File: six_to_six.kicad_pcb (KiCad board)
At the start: 2 copper layers, 114.3 x 77.5 mm, 73 parts, among them J1 BNC, J2 limiter, J3 Relay control, J4 RF Conn, K1 RY-12W-K, K2 RY-12W-K, K3 RY-12W-K, K4 RY-12W-K, K5 RY-12W-K, K6 RY-12W-K, Q1 MMBT3904, Q2 MMBT3904, Q3 MMBT3904, Q4 MMBT3904, Q5 MMBT3904, Q6 MMBT3904

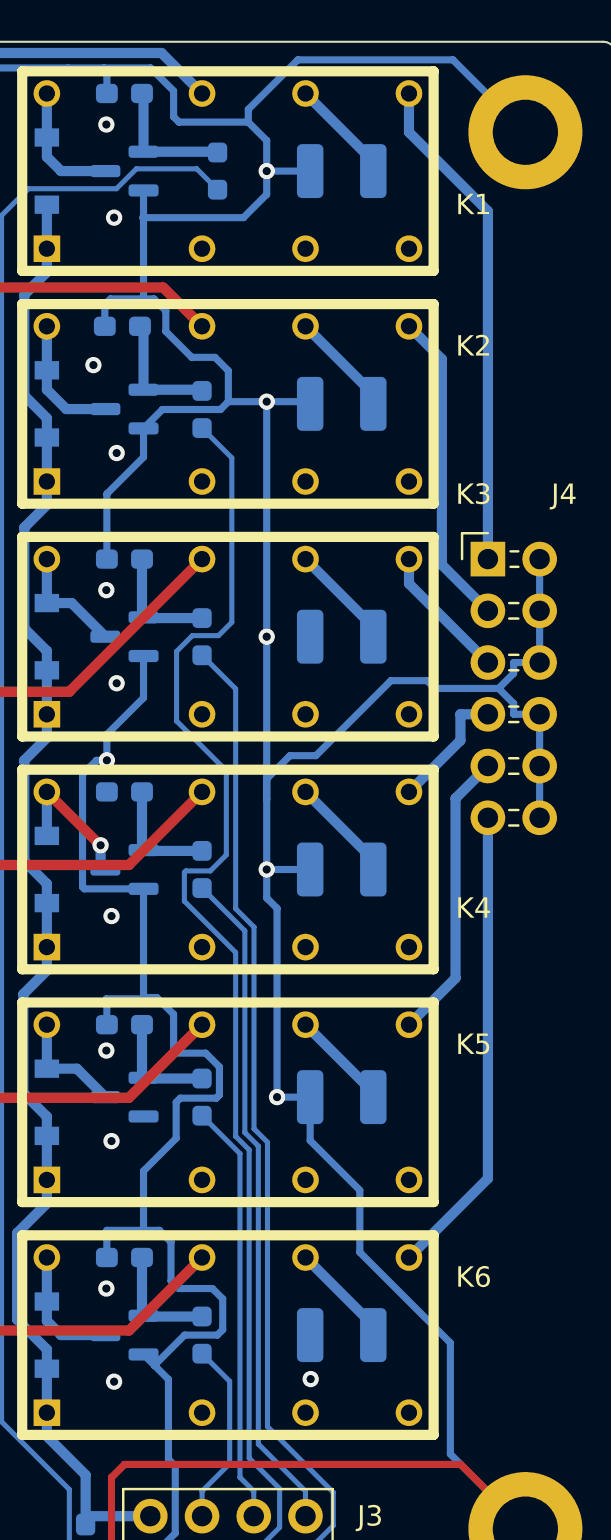
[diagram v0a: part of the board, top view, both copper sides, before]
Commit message: used both contacts on relays
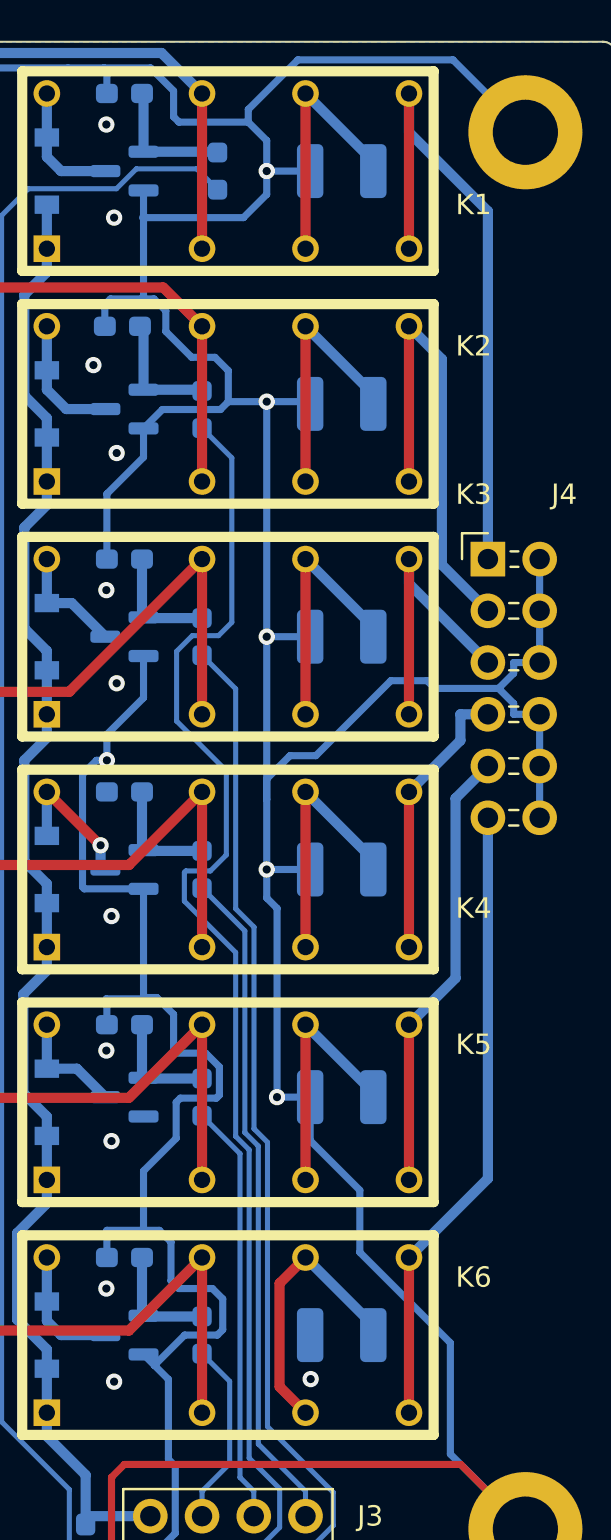
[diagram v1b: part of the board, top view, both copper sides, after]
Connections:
- K1 pad 4: unconnected-(K1-Pad4) -> /2-Way Splitter1/RF-out-1
- K1 pad 6: unconnected-(K1-Pad6) -> Net-(K1-Pad11)
- K1 pad 8: unconnected-(K1-Pad8) -> /Connectors/RF-1
- K2 pad 4: unconnected-(K2-Pad4) -> /2-Way Splitter1/RF-out-2
- K2 pad 6: unconnected-(K2-Pad6) -> Net-(K2-Pad11)
- K2 pad 8: unconnected-(K2-Pad8) -> /Connectors/RF-2
- K3 pad 4: unconnected-(K3-Pad4) -> /2-Way Splitter2/RF-out-1
- K3 pad 6: unconnected-(K3-Pad6) -> Net-(K3-Pad11)
- K3 pad 8: unconnected-(K3-Pad8) -> /Connectors/RF-3
- K4 pad 4: unconnected-(K4-Pad4) -> /2-Way Splitter2/RF-out-2
- K4 pad 6: unconnected-(K4-Pad6) -> Net-(K4-Pad11)
- K4 pad 8: unconnected-(K4-Pad8) -> /Connectors/RF-4
- K5 pad 4: unconnected-(K5-Pad4) -> /2-Way Splitter3/RF-out-1
- K5 pad 6: unconnected-(K5-Pad6) -> Net-(K5-Pad11)
- K5 pad 8: unconnected-(K5-Pad8) -> /Connectors/RF-5
- K6 pad 4: unconnected-(K6-Pad4) -> /2-Way Splitter3/RF-out-2
- K6 pad 6: unconnected-(K6-Pad6) -> Net-(K6-Pad11)
- K6 pad 8: unconnected-(K6-Pad8) -> /Connectors/RF-6
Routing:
- net Net-(K6-Pad11): track 5.19 -> 13.9 mm
- net /2-Way Splitter2/RF-out-2: track 56.6 -> 64.2 mm
- net /2-Way Splitter2/RF-out-1: track 58.2 -> 65.8 mm
- net Net-(K4-Pad11): track 5.19 -> 12.8 mm
- net Net-(K3-Pad11): track 5.19 -> 12.8 mm
- net Net-(K2-Pad11): track 5.19 -> 12.8 mm
- net /Connectors/RF-3: track 6.69 -> 14.3 mm
- net /Connectors/RF-6: track 23.2 -> 30.8 mm
- net /Connectors/RF-4: track 6.21 -> 13.8 mm
- net /Connectors/RF-2: track 15.6 -> 23.2 mm
- net /2-Way Splitter3/RF-out-2: track 53.4 -> 61.1 mm
- net /2-Way Splitter1/RF-out-2: track 48.6 -> 56.2 mm
- net /Connectors/RF-5: track 14.3 -> 21.9 mm
- net Net-(K5-Pad11): track 4.93 -> 12.6 mm
- net /Connectors/RF-1: track 24.5 -> 32.1 mm
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
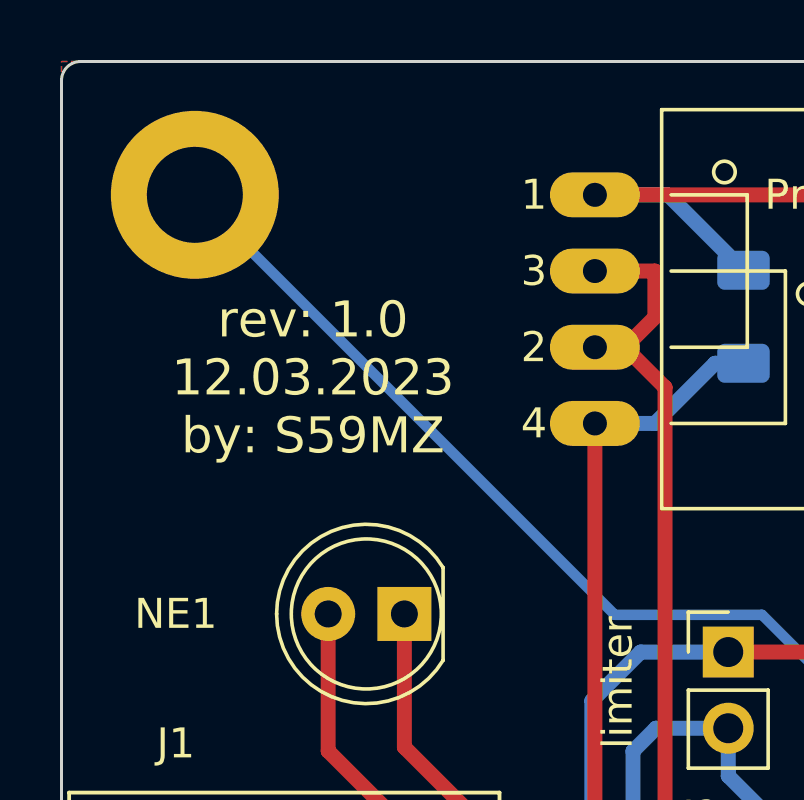
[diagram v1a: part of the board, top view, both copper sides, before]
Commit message: move mounting hole mere inside
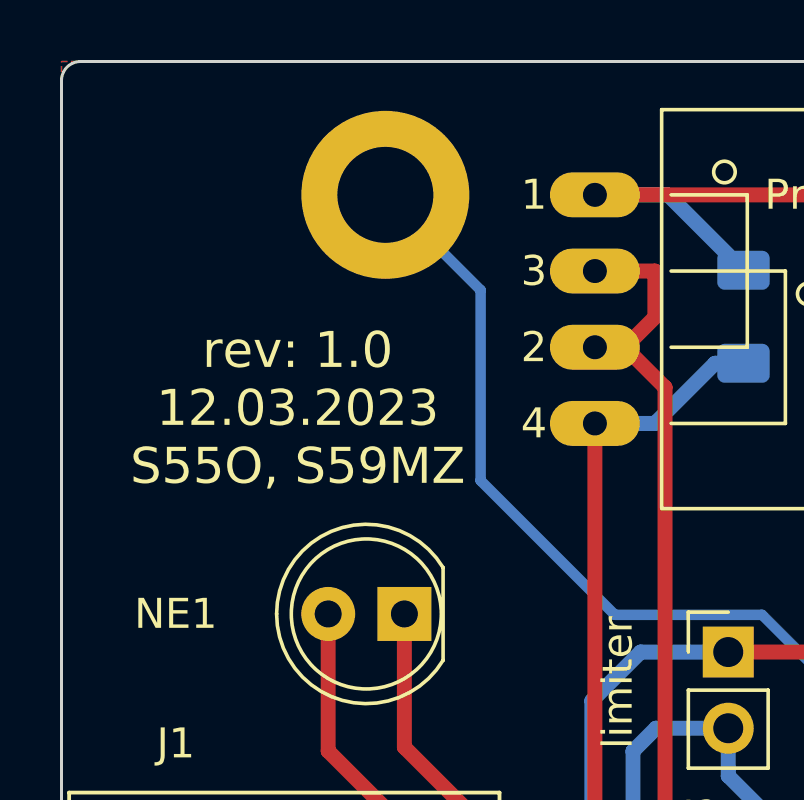
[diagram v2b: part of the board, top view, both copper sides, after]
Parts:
- moved H1 6.35 mm to (652.1, 163.8)
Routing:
- net GND: track 521.4 -> 518.7 mm
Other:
- board text added: "rev: 1.0 12.03.2023 S55O, S59MZ"
- board text removed: "rev: 1.0 12.03.2023 by: S59MZ"
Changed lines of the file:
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@@
   )
   (footprint "MountingHole:MountingHole_3.2mm_M3_DIN965_Pad" locked (layer "F.Cu")
-    (at 645.795 163.83)
+    (at 652.145 163.83)
     (descr "Mounting Hole 3.2mm, M3, DIN965")
     (tags "mounting hole 3.2mm m3 din965")
@@
   (gr_line locked (start 641.35 160.02) (end 641.35 236.22) (layer "Edge.Cuts") (width 0.1))
   (gr_line locked (start 755.65 160.02) (end 755.65 236.22) (layer "Edge.Cuts") (width 0.1))
-  (gr_text "rev: 1.0\n12.03.2023\nby: S59MZ" (at 649.732 169.926) (layer "F.SilkS")
+  (gr_text "rev: 1.0\n12.03.2023\nS55O, S59MZ" (at 649.224 170.942) (layer "F.SilkS")
     (effects (font (size 1.2 1.2) (thickness 0.15)))
   )
@@
   (segment (start 732.9915 224.3695) (end 734.477 222.884) (width 0.35) (layer "B.Cu") (net 1))
   (segment (start 751.905 189.865) (end 750.63 189.865) (width 0.35) (layer "B.Cu") (net 1))
+  (segment (start 655.32 173.355) (end 659.794 177.829) (width 0.35) (layer "B.Cu") (net 1))
   (segment (start 746.76 191.135) (end 746.379 190.754) (width 0.35) (layer "B.Cu") (net 1))
   (segment (start 737.6 163.331) (end 737.6 162.707) (width 0.35) (layer "B.Cu") (net 1))
   (segment (start 659.13 234.95) (end 684.149 234.95) (width 0.35) (layer "B.Cu") (net 1))
+  (segment (start 655.32 167.005) (end 655.32 173.355) (width 0.35) (layer "B.Cu") (net 1))
   (segment (start 738.505 164.236) (end 737.6 163.331) (width 0.35) (layer "B.Cu") (net 1))
   (segment (start 738.505 177.055) (end 738.505 188.595) (width 0.35) (layer "B.Cu") (net 1))
   (segment (start 728.742 160.671) (end 723.904 160.671) (width 0.35) (layer "B.Cu") (net 1))
-  (segment (start 645.795 163.83) (end 659.794 177.829) (width 0.35) (layer "B.Cu") (net 1))
   (segment (start 733.933 207.137) (end 733.107 206.311) (width 0.35) (layer "B.Cu") (net 1))
+  (segment (start 652.145 163.83) (end 655.32 167.005) (width 0.35) (layer "B.Cu") (net 1))
   (segment (start 730.52 160.671) (end 728.742 160.671) (width 0.35) (layer "B.Cu") (net 1))
   (segment (start 687.302 231.797) (end 687.302 226.59) (width 0.35) (layer "B.Cu") (net 1))

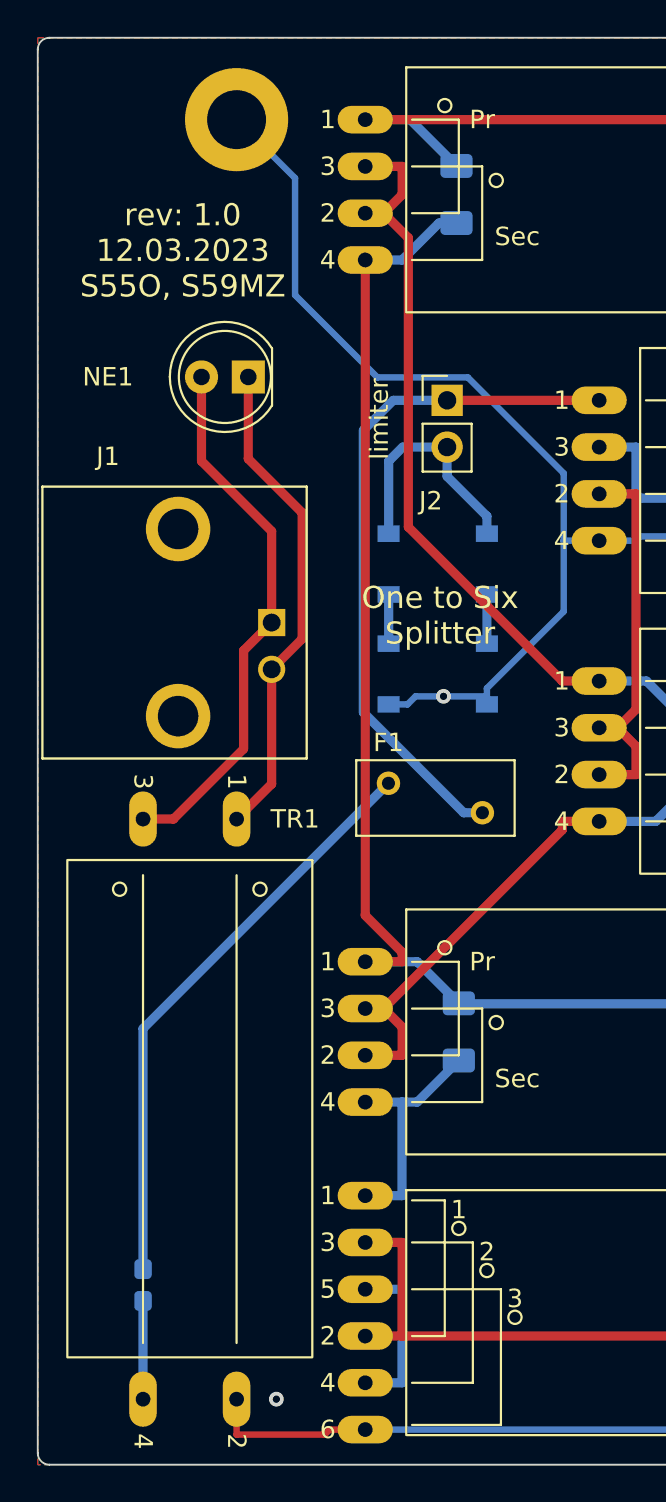
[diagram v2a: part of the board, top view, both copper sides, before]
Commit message: update CMM footprint and board name
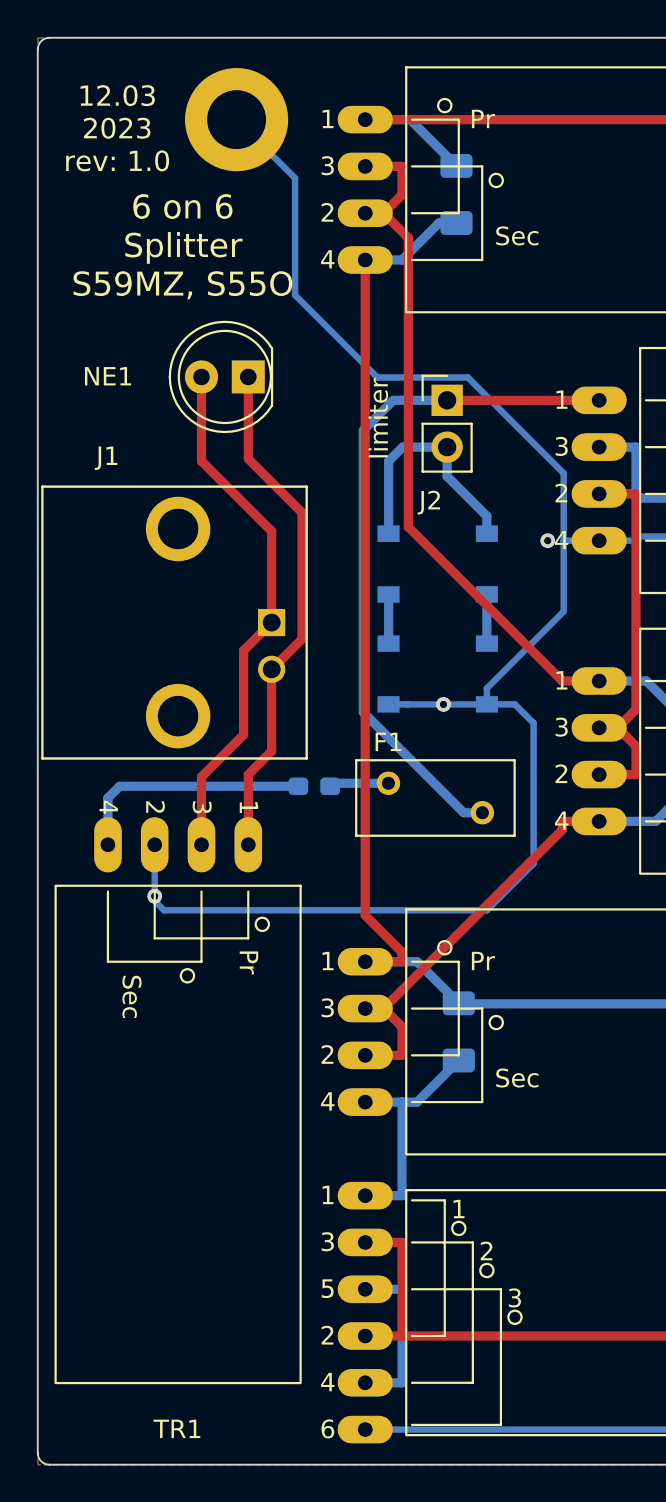
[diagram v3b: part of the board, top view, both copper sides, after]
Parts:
- J1: value BNC -> BNC 031-5431-10RFX
- TR1: footprint Components:BN-73-6802-balun -> Components:BN-73-6802-2-0
- moved C7 28.6 mm to (656.4, 200.0), turned to 0 degrees
- moved TR1 1.53 mm to (652.8, 203.2)
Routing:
- net Net-(C7-Pad2): track 31.9 -> 3.23 mm
- net GND: track 518.7 -> 545.0 mm, vias 26 -> 27
- net Net-(C7-Pad1): track 5.34 -> 13.1 mm
- net Net-(J1-Pad2): track 26.7 -> 27.8 mm
- net Net-(J1-Pad1): track 29.4 -> 28.6 mm
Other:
- board text added: "12.03 2023 rev: 1.0"
- board text added: "6 on 6 Splitter S59MZ, S55O"
- board text removed: "One to Six Splitter"
- board text removed: "rev: 1.0 12.03.2023 S55O, S59MZ"
